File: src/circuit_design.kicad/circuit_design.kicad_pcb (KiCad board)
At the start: 2 copper layers, 191.5 x 199.6 mm, 156 parts, among them J1 CONN_BAT, Q1 BT134-600E, Q2 BT134-600E, Q3 BT134-600E, Q4 BT134-600E, U1 К176ИЕ12, U10 К155ЛА4, U11 К155ЛИ1, U12 К155ЛА1, U13 К155ИЕ5, U14 К155ЛЛ1, U15 К155ЛН1, U16 К155ЛИ1, U17 К155ТВ15, U18 К155ИЕ5, U19 К155ЛП5, U2 К155ЛП10, U20 К155ИВ1, U21 К155ИД7, U22 К155ИД4, U23 К155ЛН1, U24 К155ЛП10, U25 MOC3062M, U26 MOC3062M, U27 MOC3062M, U28 MOC3062M, U29 LM7806_TO220, U3 К155ЛЕ3, U30 SC6038, U31 К155ЛЕ1, U32 К155ЛН1, U33 К155ЛИ1, U34 К155ЛА4, U35 К155ТВ15, U36 К155ТЛ2, U37 4020, U38 LM7806_TO220, U39 К155ЛН1, U4 К155ЛН1, U40 SPFT_Sliding_Switch, U41 SPFT_Sliding_Switch, U42 SPFT_Sliding_Switch, U43 SPFT_Sliding_Switch, U44 SPFT_Sliding_Switch, U45 SPFT_Sliding_Switch, U46 SPFT_Sliding_Switch, U47 SPFT_Sliding_Switch, U5 К155ЛИ1, U6 К155ЛЛ1, U7 4020, U8 ICL7660, U9 К155ИЕ5, Y1 32768

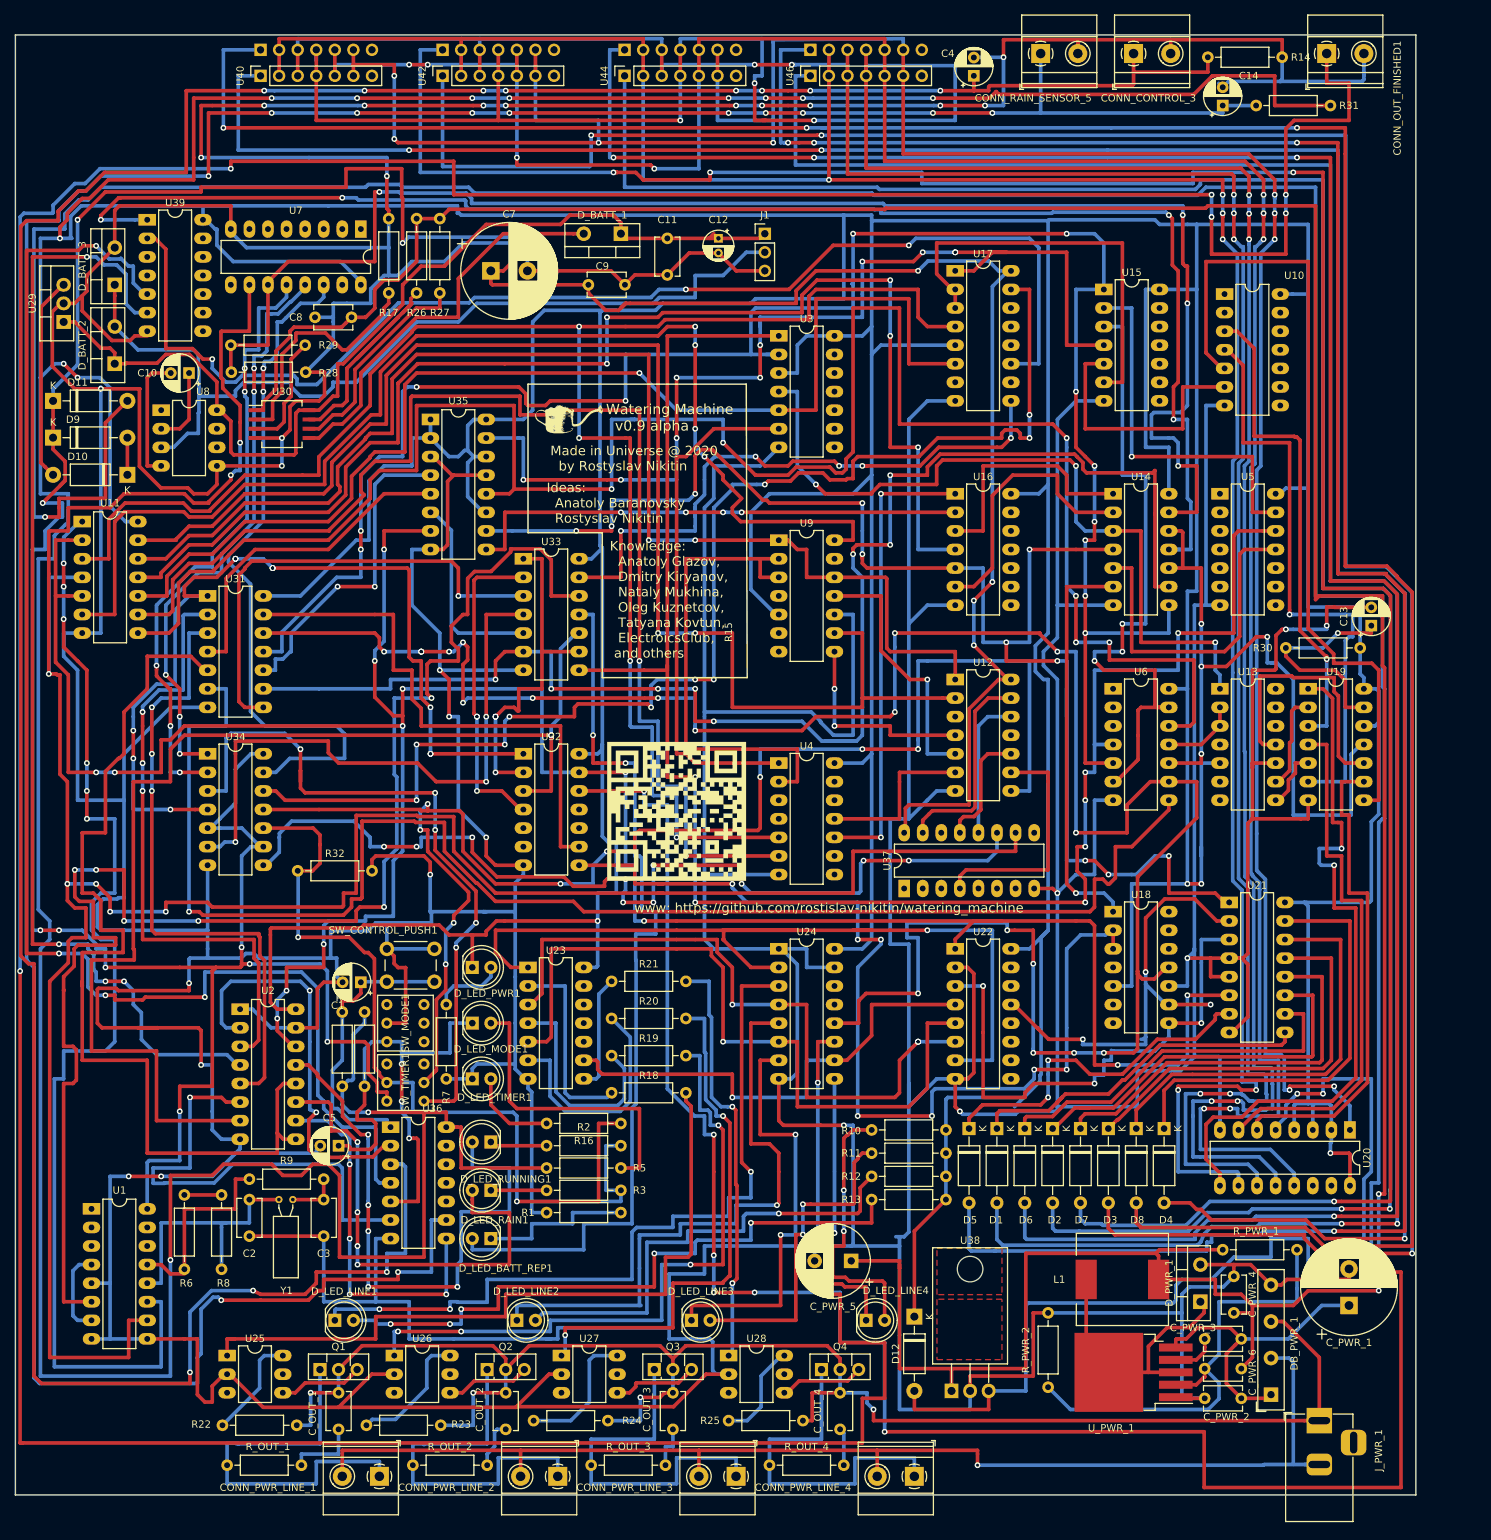
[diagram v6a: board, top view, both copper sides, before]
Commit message: 01. The labels positions was updated 02. The diode bridge footprint was updated 03. The drill holes was added/updated
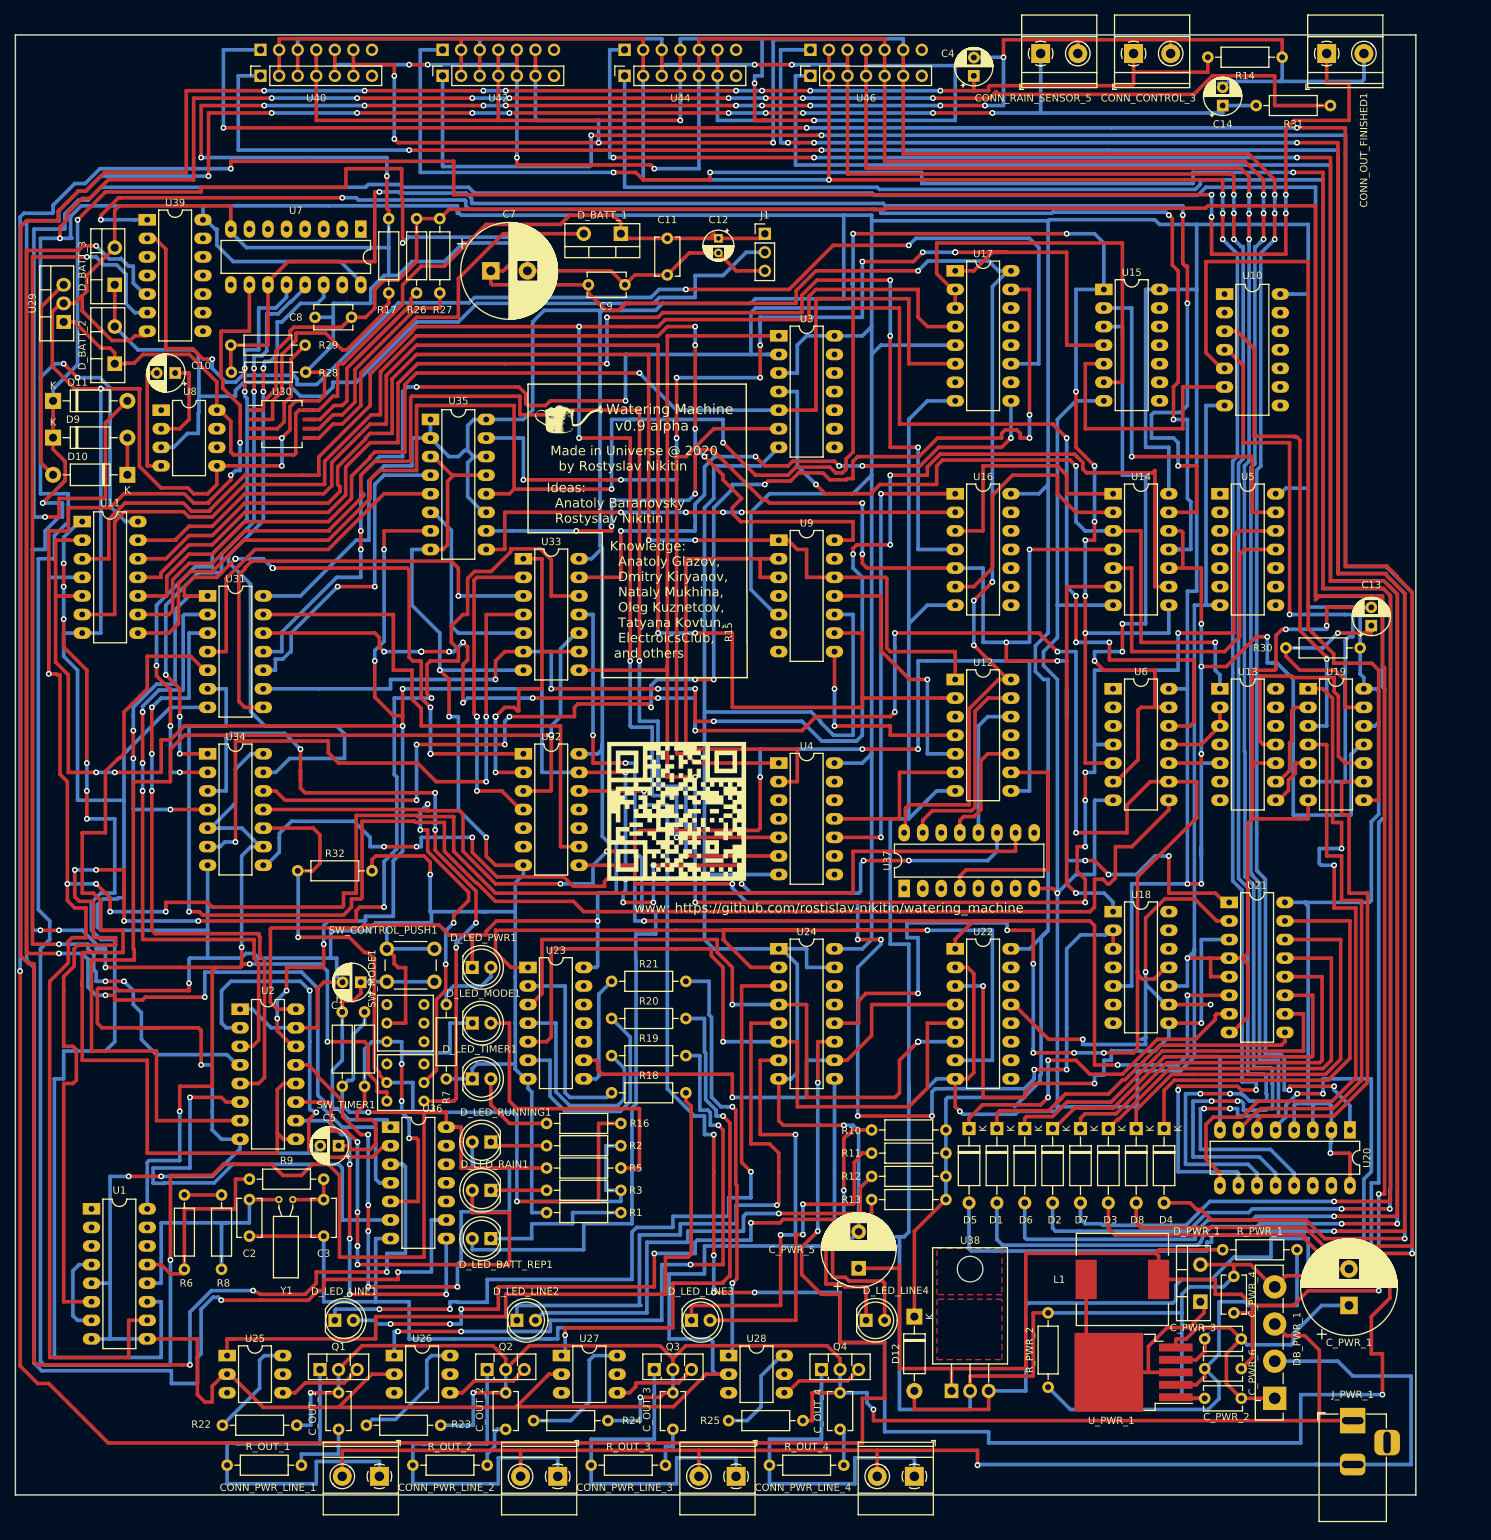
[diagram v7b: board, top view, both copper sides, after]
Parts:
- DB_PWR_1: footprint Diode_THT:Diode_Bridge_19.0x3.5x10.0mm_P5.0mm -> Diode_THT:Diode_Bridge_Vishay_GBL
- moved J_PWR_1 4.57 mm to (232.2, 178.8)
- moved C10 1.91 mm to (71.1, 35.6)
- moved C_PWR_5 1.44 mm to (164.6, 158.0), turned to 90 degrees
- moved DB_PWR_1 0.72 mm to (221.5, 175.8)
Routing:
- net GNDREF: track 169.2 -> 194.6 mm
- net /RunningInv(out): track 285.2 -> 271.2 mm
- net Net-(CONN_OUT_FINISHED1-Pad1): track 583.3 -> 577.1 mm
- net /Conn_Control_Raw: track 427.7 -> 422.9 mm
- net VAC: track 222.7 -> 227.1 mm
- net +5V: track 1784.4 -> 1781.1 mm
- net Net-(U1-Pad11): track 159.8 -> 157.2 mm
- net Net-(C_PWR_1-Pad1): track 42.2 -> 44.6 mm
- net +9V: track 459.1 -> 457.1 mm
- net Net-(C10-Pad1): track 10.7 -> 12.6 mm
- net Net-(C10-Pad2): track 17.4 -> 15.8 mm
- net Net-(D_LED_LINE1-Pad2): track 88.2 -> 87.4 mm
- net Net-(C_PWR_6-Pad2): track 63.4 -> 64.1 mm
- net GND: track 2195.9 -> 2195.3 mm
